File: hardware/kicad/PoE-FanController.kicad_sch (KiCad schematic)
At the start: 26 parts, among them J2 FAN1, J3 FAN2, J4 FAN3, J5 FAN4, J8 Waveshare_ESP32P4POEETH, U1 LM2587-12

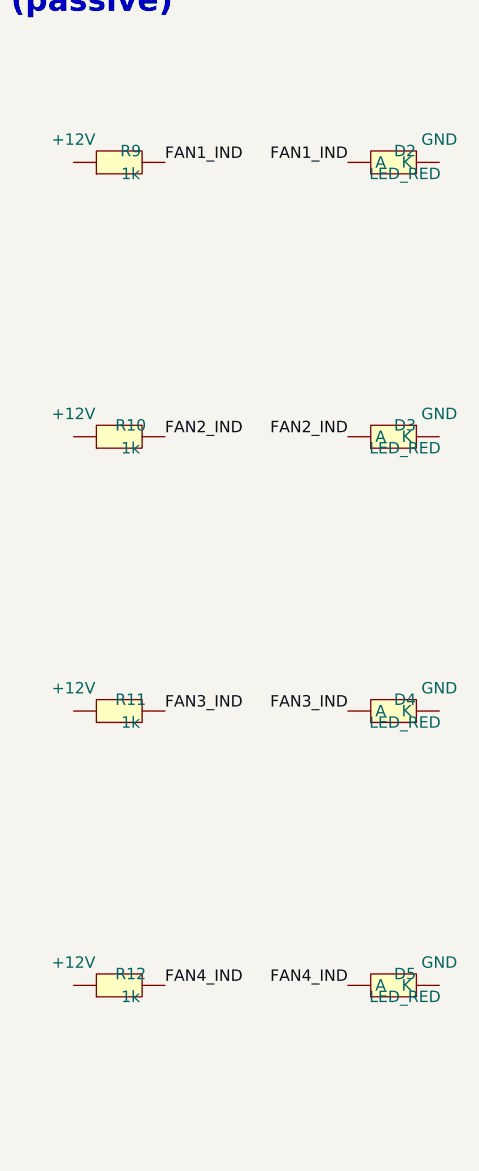
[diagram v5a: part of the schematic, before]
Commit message: hw(sch+pcb): use LED_D3.0mm THT for D2-D5 (same as LED1)
- D2-D5 footprint changed from LED_0805_2012Metric to LED_THT:LED_D3.0mm
  (matches LED1 — green 3mm THT LED, Wurth 150060GS75000)
- D1 boost diode repositioned to (38,12) to clear space above J2 for D2
- D2 placed at (50,7) — directly above J2, clear of D1 and board edge
- D3-D5 at (50,26/44/62) — directly above J3/J4/J5
- BOM: D2-D5 updated to green LED_D3.0mm, MPN 150060GS75000
- DRC: 0 real errors, 0 courtyard overlaps, 63 unconnected (routing pending)

Co-authored-by: Copilot <223556219+Copilot@users.noreply.github.com>
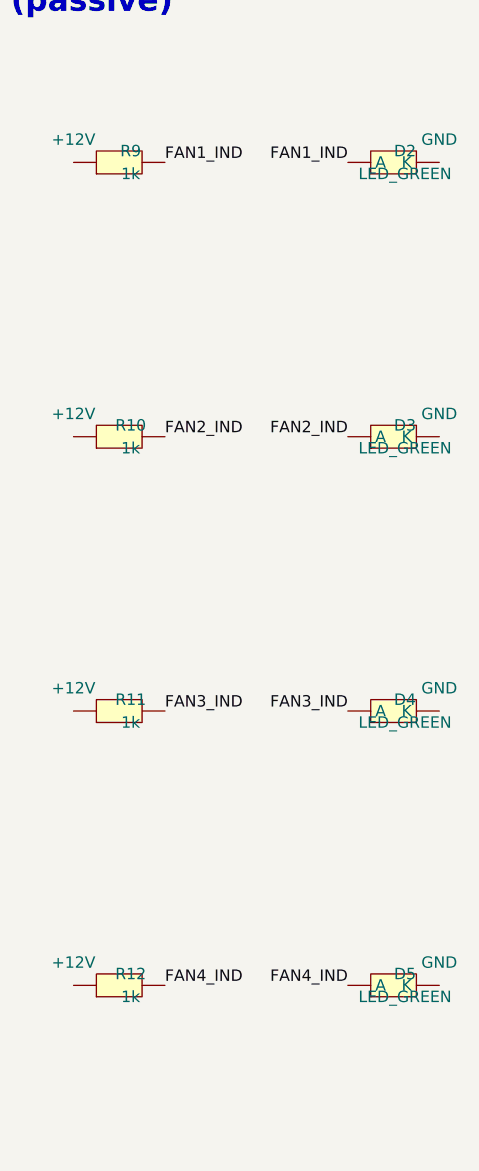
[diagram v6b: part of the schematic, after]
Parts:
- D2, D3, D4, D5: value LED_RED -> LED_GREEN; footprint LED_SMD:LED_0805_2012Metric -> LED_THT:LED_D3.0mm
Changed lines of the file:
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@@
       (at 405.1300 80.0100 0)
       (effects (font (size 1.27 1.27))))
-    (property "Value" "LED_RED"
+    (property "Value" "LED_GREEN"
       (at 405.1300 82.5500 0)
       (effects (font (size 1.27 1.27))))
-    (property "Footprint" "LED_SMD:LED_0805_2012Metric"
+    (property "Footprint" "LED_THT:LED_D3.0mm"
       (at 403.8600 81.2800 0)
       (hide yes)
@@
       (at 405.1300 110.4900 0)
       (effects (font (size 1.27 1.27))))
-    (property "Value" "LED_RED"
+    (property "Value" "LED_GREEN"
       (at 405.1300 113.0300 0)
       (effects (font (size 1.27 1.27))))
-    (property "Footprint" "LED_SMD:LED_0805_2012Metric"
+    (property "Footprint" "LED_THT:LED_D3.0mm"
       (at 403.8600 111.7600 0)
       (hide yes)
@@
       (at 405.1300 140.9700 0)
       (effects (font (size 1.27 1.27))))
-    (property "Value" "LED_RED"
+    (property "Value" "LED_GREEN"
       (at 405.1300 143.5100 0)
       (effects (font (size 1.27 1.27))))
-    (property "Footprint" "LED_SMD:LED_0805_2012Metric"
+    (property "Footprint" "LED_THT:LED_D3.0mm"
       (at 403.8600 142.2400 0)
       (hide yes)
@@
       (at 405.1300 171.4500 0)
       (effects (font (size 1.27 1.27))))
-    (property "Value" "LED_RED"
+    (property "Value" "LED_GREEN"
       (at 405.1300 173.9900 0)
       (effects (font (size 1.27 1.27))))
-    (property "Footprint" "LED_SMD:LED_0805_2012Metric"
+    (property "Footprint" "LED_THT:LED_D3.0mm"
       (at 403.8600 172.7200 0)
       (hide yes)

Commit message: hw: replace all 0402 resistors with 0805 for hand-solderability (issue #90)
- R3, R4, R5-R8, R9-R12: footprint changed from R_0402_1005Metric to R_0805_2012Metric
- All pad geometries, courtyards, silkscreen updated to 0805 dimensions
- BOM: Yageo MPN updated to RC0805FR-07xxx equivalents
- D1 repositioned to (48, 2.5) to maintain clearance from L1 pad 2 at (43.16, 3)
  and from fan indicator LEDs above fan headers
- DRC: 0 real errors, 0 courtyard overlaps, 63 unconnected (routing pending)
- ERC: 0 errors

Co-authored-by: Copilot <223556219+Copilot@users.noreply.github.com>
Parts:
- R10, R11, R12, R3, R4, R5, R6, R7, R8, R9: footprint Resistor_SMD:R_0402_1005Metric -> Resistor_SMD:R_0805_2012Metric
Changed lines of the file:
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@@
       (at 280.6700 82.5500 0)
       (effects (font (size 1.27 1.27))))
-    (property "Footprint" "Resistor_SMD:R_0402_1005Metric"
+    (property "Footprint" "Resistor_SMD:R_0805_2012Metric"
       (at 279.4000 81.2800 0)
       (hide yes)
@@
       (at 280.6700 113.0300 0)
       (effects (font (size 1.27 1.27))))
-    (property "Footprint" "Resistor_SMD:R_0402_1005Metric"
+    (property "Footprint" "Resistor_SMD:R_0805_2012Metric"
       (at 279.4000 111.7600 0)
       (hide yes)
@@
       (at 280.6700 143.5100 0)
       (effects (font (size 1.27 1.27))))
-    (property "Footprint" "Resistor_SMD:R_0402_1005Metric"
+    (property "Footprint" "Resistor_SMD:R_0805_2012Metric"
       (at 279.4000 142.2400 0)
       (hide yes)
@@
       (at 280.6700 173.9900 0)
       (effects (font (size 1.27 1.27))))
-    (property "Footprint" "Resistor_SMD:R_0402_1005Metric"
+    (property "Footprint" "Resistor_SMD:R_0805_2012Metric"
       (at 279.4000 172.7200 0)
       (hide yes)
@@
       (at 374.6500 82.5500 0)
       (effects (font (size 1.27 1.27))))
-    (property "Footprint" "Resistor_SMD:R_0402_1005Metric"
+    (property "Footprint" "Resistor_SMD:R_0805_2012Metric"
       (at 373.3800 81.2800 0)
       (hide yes)
@@
       (at 374.6500 113.0300 0)
       (effects (font (size 1.27 1.27))))
-    (property "Footprint" "Resistor_SMD:R_0402_1005Metric"
+    (property "Footprint" "Resistor_SMD:R_0805_2012Metric"
       (at 373.3800 111.7600 0)
       (hide yes)
@@
       (at 374.6500 143.5100 0)
       (effects (font (size 1.27 1.27))))
-    (property "Footprint" "Resistor_SMD:R_0402_1005Metric"
+    (property "Footprint" "Resistor_SMD:R_0805_2012Metric"
       (at 373.3800 142.2400 0)
       (hide yes)
@@
       (at 374.6500 173.9900 0)
       (effects (font (size 1.27 1.27))))
-    (property "Footprint" "Resistor_SMD:R_0402_1005Metric"
+    (property "Footprint" "Resistor_SMD:R_0805_2012Metric"
       (at 373.3800 172.7200 0)
       (hide yes)
@@
       (at 158.7500 229.8700 0)
       (effects (font (size 1.27 1.27))))
-    (property "Footprint" "Resistor_SMD:R_0402_1005Metric"
+    (property "Footprint" "Resistor_SMD:R_0805_2012Metric"
       (at 157.4800 228.6000 0)
       (hide yes)
@@
       (at 158.7500 265.4300 0)
       (effects (font (size 1.27 1.27))))
-    (property "Footprint" "Resistor_SMD:R_0402_1005Metric"
+    (property "Footprint" "Resistor_SMD:R_0805_2012Metric"
       (at 157.4800 264.1600 0)
       (hide yes)

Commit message: hw: replace all SMD resistors with P7.62mm THT axial (issue #90)
- All 10 resistors (R3, R4, R5-R8, R9-R12) changed from 0805 SMD to
  Resistor_THT:R_Axial_DIN0207_L6.3mm_D2.5mm_P7.62mm_Horizontal
  (1/4W axial THT — hand-solderable without microscope)
- BOM: Yageo MFR-25FBF52 series (1/4W 1% axial THT)
- PCB footprint anchors adjusted to keep pad 2 clear of fan headers/LEDs:
    R5-R8 (TACH pull-ups):  anchor (35, 12/30/48/66), pad2 at X=42.62
    R9-R12 (LED current):   anchor (36, 7/25/43/61),  pad2 at X=43.62
    R3, R4: anchor unchanged at (25, 20) and (25, 24)
- DRC: 0 real errors, 0 courtyard overlaps, 63 unconnected (routing pending)

Co-authored-by: Copilot <223556219+Copilot@users.noreply.github.com>
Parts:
- R10, R11, R12, R3, R4, R5, R6, R7, R8, R9: footprint Resistor_SMD:R_0805_2012Metric -> Resistor_THT:R_Axial_DIN0207_L6.3mm_D2.5mm_P7.62mm_Horizontal
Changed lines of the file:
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@@
       (at 280.6700 82.5500 0)
       (effects (font (size 1.27 1.27))))
-    (property "Footprint" "Resistor_SMD:R_0805_2012Metric"
+    (property "Footprint" "Resistor_THT:R_Axial_DIN0207_L6.3mm_D2.5mm_P7.62mm_Horizontal"
       (at 279.4000 81.2800 0)
       (hide yes)
@@
       (at 280.6700 113.0300 0)
       (effects (font (size 1.27 1.27))))
-    (property "Footprint" "Resistor_SMD:R_0805_2012Metric"
+    (property "Footprint" "Resistor_THT:R_Axial_DIN0207_L6.3mm_D2.5mm_P7.62mm_Horizontal"
       (at 279.4000 111.7600 0)
       (hide yes)
@@
       (at 280.6700 143.5100 0)
       (effects (font (size 1.27 1.27))))
-    (property "Footprint" "Resistor_SMD:R_0805_2012Metric"
+    (property "Footprint" "Resistor_THT:R_Axial_DIN0207_L6.3mm_D2.5mm_P7.62mm_Horizontal"
       (at 279.4000 142.2400 0)
       (hide yes)
@@
       (at 280.6700 173.9900 0)
       (effects (font (size 1.27 1.27))))
-    (property "Footprint" "Resistor_SMD:R_0805_2012Metric"
+    (property "Footprint" "Resistor_THT:R_Axial_DIN0207_L6.3mm_D2.5mm_P7.62mm_Horizontal"
       (at 279.4000 172.7200 0)
       (hide yes)
@@
       (at 374.6500 82.5500 0)
       (effects (font (size 1.27 1.27))))
-    (property "Footprint" "Resistor_SMD:R_0805_2012Metric"
+    (property "Footprint" "Resistor_THT:R_Axial_DIN0207_L6.3mm_D2.5mm_P7.62mm_Horizontal"
       (at 373.3800 81.2800 0)
       (hide yes)
@@
       (at 374.6500 113.0300 0)
       (effects (font (size 1.27 1.27))))
-    (property "Footprint" "Resistor_SMD:R_0805_2012Metric"
+    (property "Footprint" "Resistor_THT:R_Axial_DIN0207_L6.3mm_D2.5mm_P7.62mm_Horizontal"
       (at 373.3800 111.7600 0)
       (hide yes)
@@
       (at 374.6500 143.5100 0)
       (effects (font (size 1.27 1.27))))
-    (property "Footprint" "Resistor_SMD:R_0805_2012Metric"
+    (property "Footprint" "Resistor_THT:R_Axial_DIN0207_L6.3mm_D2.5mm_P7.62mm_Horizontal"
       (at 373.3800 142.2400 0)
       (hide yes)
@@
       (at 374.6500 173.9900 0)
       (effects (font (size 1.27 1.27))))
-    (property "Footprint" "Resistor_SMD:R_0805_2012Metric"
+    (property "Footprint" "Resistor_THT:R_Axial_DIN0207_L6.3mm_D2.5mm_P7.62mm_Horizontal"
       (at 373.3800 172.7200 0)
       (hide yes)
@@
       (at 158.7500 229.8700 0)
       (effects (font (size 1.27 1.27))))
-    (property "Footprint" "Resistor_SMD:R_0805_2012Metric"
+    (property "Footprint" "Resistor_THT:R_Axial_DIN0207_L6.3mm_D2.5mm_P7.62mm_Horizontal"
       (at 157.4800 228.6000 0)
       (hide yes)
@@
       (at 158.7500 265.4300 0)
       (effects (font (size 1.27 1.27))))
-    (property "Footprint" "Resistor_SMD:R_0805_2012Metric"
+    (property "Footprint" "Resistor_THT:R_Axial_DIN0207_L6.3mm_D2.5mm_P7.62mm_Horizontal"
       (at 157.4800 264.1600 0)
       (hide yes)
